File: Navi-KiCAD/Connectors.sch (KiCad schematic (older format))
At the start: 4 parts, among them J1 AXK5S80047YG, J2 AXK5S80047YG, J3 473460001, U13 NUF2042XV6T1G

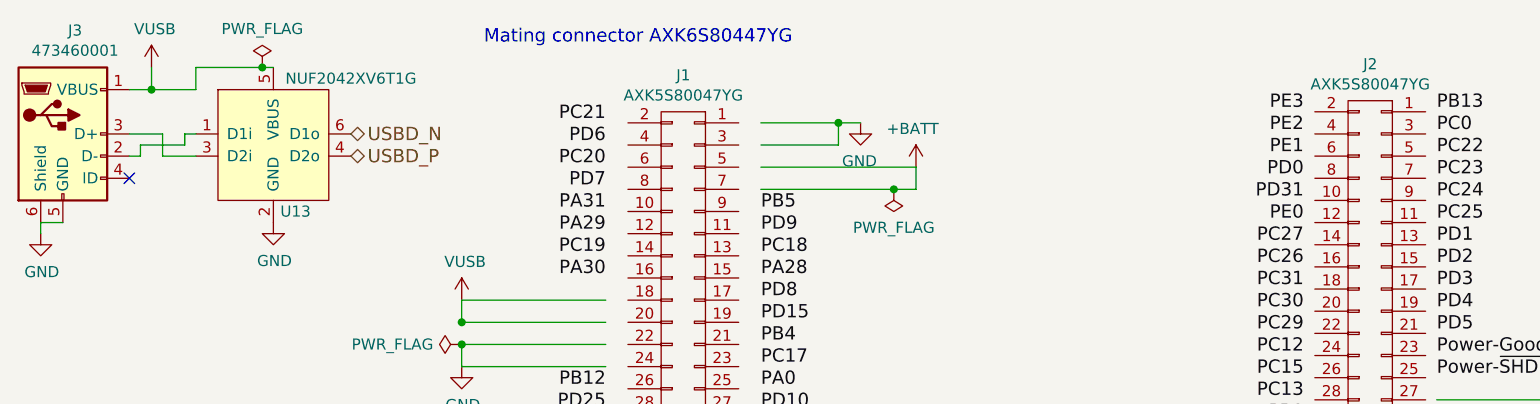
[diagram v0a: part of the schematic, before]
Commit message: Completed key routing.
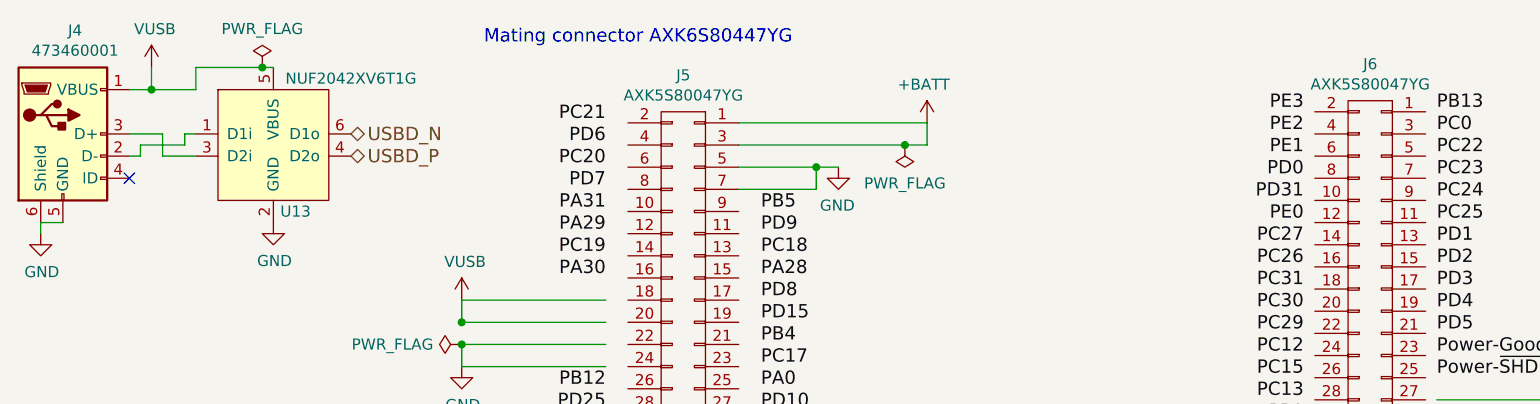
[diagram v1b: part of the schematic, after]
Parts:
- renumbered J3 to J4, J1 to J5, J2 to J6
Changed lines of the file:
@@
 $EndDescr
 $Comp
-L USB_OTG J3
+L USB_OTG J4
 U 1 1 58B53909
 P 1200 1450
-F 0 "J3" H 1255 1917 50  0000 C CNN
+F 0 "J4" H 1255 1917 50  0000 C CNN
 F 1 "473460001" H 1255 1826 50  0000 C CNN
 F 2 "Connectors:USB_Micro-B_0473460001" H -3450 -1350 50  0001 C CNN
@@
 $EndComp
 $Comp
-L CONN_02X40 J1
+L CONN_02X40 J5
 U 1 1 58B54687
 P 4000 3350
-F 0 "J1" H 4000 5515 50  0000 C CNN
+F 0 "J5" H 4000 5515 50  0000 C CNN
 F 1 "AXK5S80047YG" H 4000 5424 50  0000 C CNN
 F 2 "Connectors:AXK5S80047YG" H -550 200 50  0001 C CNN
@@
 Mating connector AXK6S80447YG
 $Comp
-L CONN_02X40 J2
+L CONN_02X40 J6
 U 1 1 58B24420
 P 7100 3300
-F 0 "J2" H 7100 5465 50  0000 C CNN
+F 0 "J6" H 7100 5465 50  0000 C CNN
 F 1 "AXK5S80047YG" H 7100 5374 50  0000 C CNN
 F 2 "Connectors:AXK5S80047YG" H 2550 150 50  0001 C CNN
@@
 L +BATT #PWR0154
 U 1 1 58DB91A4
-P 5050 1600
-F 0 "#PWR0154" H 4000 -1300 50  0001 C CNN
-F 1 "+BATT" H 5065 1773 50  0000 C CNN
-F 2 "" H 4000 -1150 50  0001 C CNN
-F 3 "" H 4000 -1150 50  0001 C CNN
-	1    5050 1600
+P 5100 1400
+F 0 "#PWR0154" H 4050 -1500 50  0001 C CNN
+F 1 "+BATT" H 5115 1573 50  0000 C CNN
+F 2 "" H 4050 -1350 50  0001 C CNN
+F 3 "" H 4050 -1350 50  0001 C CNN
+	1    5100 1400
 	-1   0    0    -1
 $EndComp
@@
 L GND #PWR0155
 U 1 1 58DD26EA
-P 4800 1400
-F 0 "#PWR0155" H 850 -2300 50  0001 C CNN
-F 1 "GND" H 4805 1227 50  0000 C CNN
-F 2 "" H 850 -2050 50  0001 C CNN
-F 3 "" H 850 -2050 50  0001 C CNN
-	1    4800 1400
+P 4700 1600
+F 0 "#PWR0155" H 750 -2100 50  0001 C CNN
+F 1 "GND" H 4705 1427 50  0000 C CNN
+F 2 "" H 750 -1850 50  0001 C CNN
+F 3 "" H 750 -1850 50  0001 C CNN
+	1    4700 1600
 	-1   0    0    -1
 $EndComp
@@
 PC7
 Wire Wire Line
-	4700 1500 4350 1500
-Wire Wire Line
-	4350 1400 4800 1400
-Wire Wire Line
-	4700 1400 4700 1500
-Wire Wire Line
-	4350 1700 5050 1700
-Wire Wire Line
-	5050 1700 5050 1600
-Connection ~ 4700 1400
+	4600 1700 4250 1700
+Wire Wire Line
+	4250 1600 4700 1600
+Wire Wire Line
+	4600 1600 4600 1700
+Wire Wire Line
+	4250 1500 5100 1500
+Wire Wire Line
+	5100 1500 5100 1400
+Connection ~ 4600 1600
 Text Label 7400 3450 0    60   ~ 0
 900-DIO-10
@@
 L PWR_FLAG #FLG0158
 U 1 1 58BE5320
-P 4950 1700
-F 0 "#FLG0158" H -700 275 50  0001 C CNN
-F 1 "PWR_FLAG" H 4950 1873 50  0000 C CNN
-F 2 "" H -700 200 50  0001 C CNN
-F 3 "" H -700 200 50  0001 C CNN
-	1    4950 1700
+P 5000 1500
+F 0 "#FLG0158" H -650 75  50  0001 C CNN
+F 1 "PWR_FLAG" H 5000 1673 50  0000 C CNN
+F 2 "" H -650 0   50  0001 C CNN
+F 3 "" H -650 0   50  0001 C CNN
+	1    5000 1500
 	-1   0    0    1
 $EndComp
-Connection ~ 4950 1700
+Connection ~ 5000 1500
 $Comp
 L PWR_FLAG #FLG0159
@@
 	1750 1450 1800 1450
 Wire Wire Line
-	5050 1600 4350 1600
+	5100 1400 4250 1400
 $EndSCHEMATC

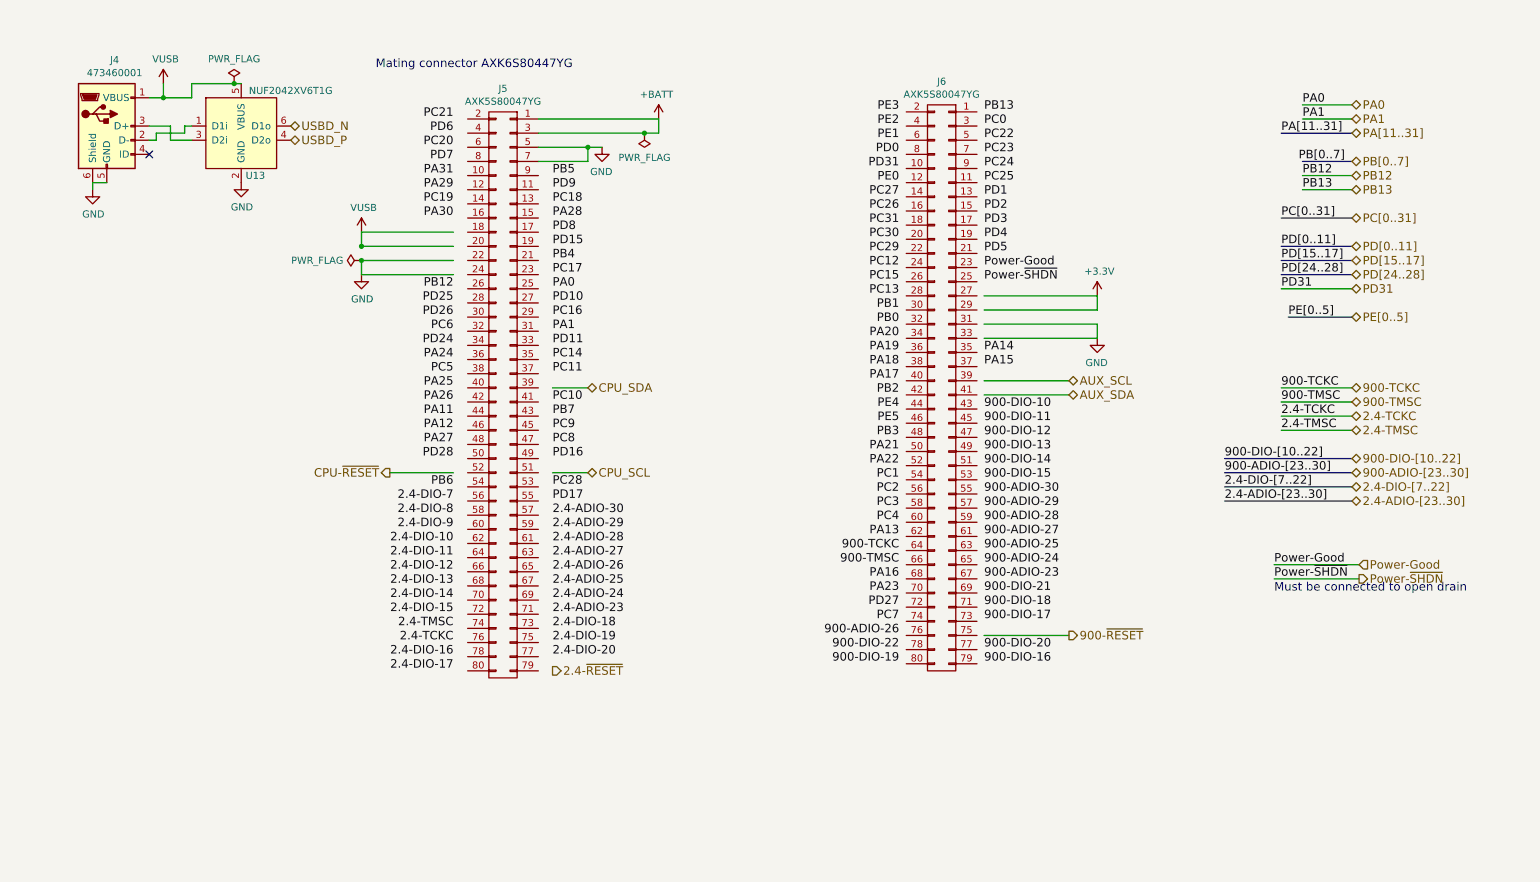
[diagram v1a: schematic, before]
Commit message: Some more GNC processor routing
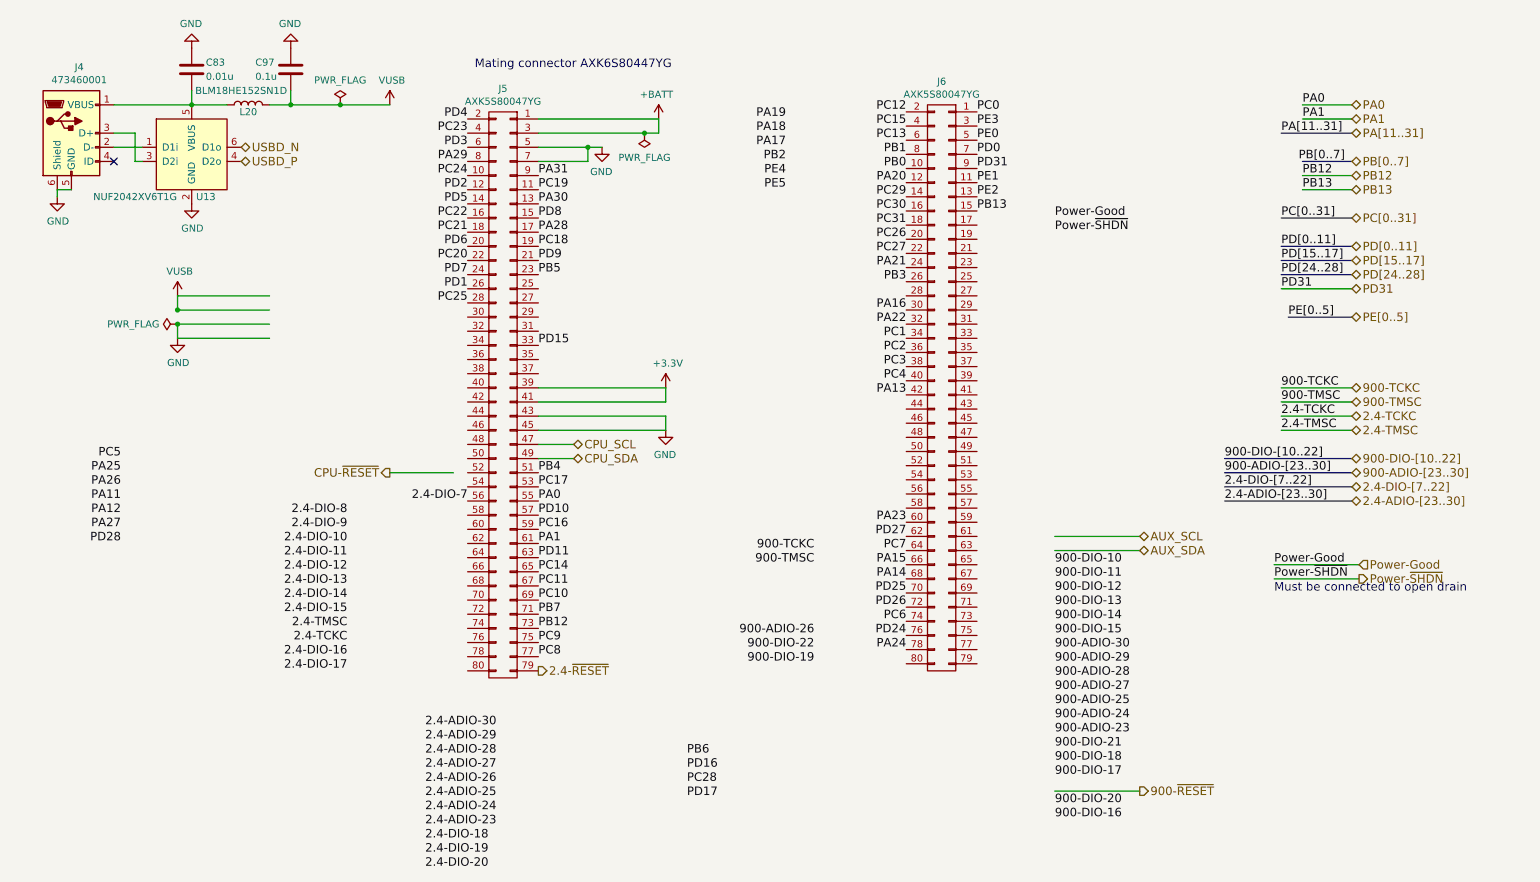
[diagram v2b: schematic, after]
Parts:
- added C83: 0.01u, Capacitors_SMD:C_0402, symbol C
- added C97: 0.1u, Capacitors_SMD:C_0402, symbol C
- added L20: BLM18HE152SN1D, Inductors_SMD:L_0603, symbol L
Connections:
- wire segments 49 -> 46
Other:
- moved on the sheet: J4, U13

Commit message: Additional routing
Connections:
- net labels removed: Power-Good
- wire segments 46 -> 42
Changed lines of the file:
@@
 Text HLabel 2150 1600 2    60   BiDi ~ 0
 USBD_N
-Text HLabel 3200 3900 0    60   Output ~ 0
+Text HLabel 2450 4050 0    60   Output ~ 0
 CPU-~RESET
-Text HLabel 8500 6150 2    60   Output ~ 0
+Text HLabel 8950 6100 2    60   Output ~ 0
 900-~RESET
 Text HLabel 4250 5300 2    60   Output ~ 0
@@
 Text HLabel 10000 2600 2    60   BiDi ~ 0
 PD31
-Text HLabel 8500 4450 2    60   BiDi ~ 0
+Text HLabel 5650 2250 2    60   BiDi ~ 0
 AUX_SDA
-Text HLabel 8500 4350 2    60   BiDi ~ 0
+Text HLabel 5650 2150 2    60   BiDi ~ 0
 AUX_SCL
 Text HLabel 4500 3800 2    60   BiDi ~ 0
@@
 Text HLabel 10000 4100 2    60   BiDi ~ 0
 2.4-ADIO-[23..30]
-Wire Wire Line
-	9450 4550 10050 4550
-Text Label 9450 4550 0    60   ~ 0
-Power-Good
-Text HLabel 10050 4550 2    60   Input ~ 0
-Power-Good
 Text Label 9450 4650 0    60   ~ 0
 Power-~SHDN
@@
 	-1   0    0    -1
 $EndComp
-Text Label 7900 5250 0    60   ~ 0
+Text Label 7350 5150 0    60   ~ 0
 900-ADIO-29
-Text Label 7900 5150 0    60   ~ 0
+Text Label 7350 5050 0    60   ~ 0
 900-ADIO-30
-Text Label 7900 5350 0    60   ~ 0
+Text Label 7350 5250 0    60   ~ 0
 900-ADIO-28
-Text Label 6200 5050 2    60   ~ 0
+Text Label 7350 4550 0    60   ~ 0
 900-ADIO-26
-Text Label 7900 5650 0    60   ~ 0
+Text Label 7350 4350 0    60   ~ 0
 900-ADIO-24
-Text Label 7900 5750 0    60   ~ 0
+Text Label 7350 4250 0    60   ~ 0
 900-ADIO-23
-Text Label 7900 5450 0    60   ~ 0
+Text Label 7350 4150 0    60   ~ 0
 900-ADIO-27
-Text Label 7900 5550 0    60   ~ 0
+Text Label 7350 4650 0    60   ~ 0
 900-ADIO-25
-Text Label 2900 4200 2    60   ~ 0
+Text Label 3750 4000 2    60   ~ 0
 2.4-DIO-8
-Text Label 2900 4300 2    60   ~ 0
+Text Label 3750 3900 2    60   ~ 0
 2.4-DIO-9
-Text Label 2900 4400 2    60   ~ 0
+Text Label 3750 3800 2    60   ~ 0
 2.4-DIO-10
-Text Label 2900 4500 2    60   ~ 0
+Text Label 3750 4300 2    60   ~ 0
 2.4-DIO-11
-Text Label 2900 4600 2    60   ~ 0
+Text Label 3750 4500 2    60   ~ 0
 2.4-DIO-12
-Text Label 2900 4700 2    60   ~ 0
+Text Label 3750 4700 2    60   ~ 0
 2.4-DIO-13
-Text Label 2900 4800 2    60   ~ 0
+Text Label 3750 4900 2    60   ~ 0
 2.4-DIO-14
-Text Label 2900 4900 2    60   ~ 0
+Text Label 3750 5300 2    60   ~ 0
 2.4-DIO-15
-Text Label 2900 5100 2    60   ~ 0
+Text Label 3750 5100 2    60   ~ 0
 2.4-TCKC
-Text Label 2900 5000 2    60   ~ 0
+Text Label 3750 5200 2    60   ~ 0
 2.4-TMSC
-Text Label 2900 5200 2    60   ~ 0
+Text Label 3750 5000 2    60   ~ 0
 2.4-DIO-16
-Text Label 2900 5300 2    60   ~ 0
+Text Label 3750 4800 2    60   ~ 0
 2.4-DIO-17
-Text Label 3450 6500 0    60   ~ 0
+Text Label 3750 4600 2    60   ~ 0
 2.4-DIO-18
-Text Label 3450 6600 0    60   ~ 0
+Text Label 3750 4400 2    60   ~ 0
 2.4-DIO-19
-Text Label 3450 6700 0    60   ~ 0
+Text Label 3750 4200 2    60   ~ 0
 2.4-DIO-20
-Text Label 3450 6400 0    60   ~ 0
+Text Label 1250 3750 2    60   ~ 0
 2.4-ADIO-23
-Text Label 3450 6300 0    60   ~ 0
+Text Label 1250 3850 2    60   ~ 0
 2.4-ADIO-24
-Text Label 3450 6200 0    60   ~ 0
+Text Label 1250 3950 2    60   ~ 0
 2.4-ADIO-25
-Text Label 3450 6100 0    60   ~ 0
+Text Label 1250 4050 2    60   ~ 0
 2.4-ADIO-26
-Text Label 3450 6000 0    60   ~ 0
+Text Label 1250 4150 2    60   ~ 0
 2.4-ADIO-27
-Text Label 3450 5900 0    60   ~ 0
+Text Label 1250 4250 2    60   ~ 0
 2.4-ADIO-28
-Text Label 3450 5800 0    60   ~ 0
+Text Label 1250 4350 2    60   ~ 0
 2.4-ADIO-29
-Text Label 3450 5700 0    60   ~ 0
+Text Label 1250 4450 2    60   ~ 0
 2.4-ADIO-30
 Text Label 5300 6200 0    60   ~ 0
@@
 Text Label 6850 1850 2    60   ~ 0
 PA20
-Text Label 6000 1400 2    60   ~ 0
+Text Label 5650 1450 2    60   ~ 0
 PA19
-Text Label 6000 1500 2    60   ~ 0
+Text Label 5650 1550 2    60   ~ 0
 PA18
-Text Label 6000 1600 2    60   ~ 0
+Text Label 5650 1650 2    60   ~ 0
 PA17
-Text Label 6000 1700 2    60   ~ 0
+Text Label 5650 1750 2    60   ~ 0
 PB2
-Text Label 6000 1800 2    60   ~ 0
+Text Label 5650 1850 2    60   ~ 0
 PE4
-Text Label 6000 1900 2    60   ~ 0
+Text Label 6850 2650 2    60   ~ 0
 PE5
 Text Label 6850 2550 2    60   ~ 0
@@
 Text Label 6850 2450 2    60   ~ 0
 PA21
-Text Label 7900 6350 0    60   ~ 0
+Text Label 8350 6300 0    60   ~ 0
 900-DIO-16
-Text Label 7900 6250 0    60   ~ 0
+Text Label 8350 6200 0    60   ~ 0
 900-DIO-20
 Wire Wire Line
-	7900 6150 8500 6150
-Text Label 7900 5850 0    60   ~ 0
+	8350 6100 8950 6100
+Text Label 7350 3950 0    60   ~ 0
 900-DIO-21
-Text Label 7900 6050 0    60   ~ 0
+Text Label 8350 6000 0    60   ~ 0
 900-DIO-17
-Text Label 7900 5950 0    60   ~ 0
+Text Label 8350 5900 0    60   ~ 0
 900-DIO-18
-Text Label 6200 5150 2    60   ~ 0
+Text Label 7350 4050 0    60   ~ 0
 900-DIO-22
-Text Label 6200 5250 2    60   ~ 0
+Text Label 8150 6300 2    60   ~ 0
 900-DIO-19
 Text Label 3750 2700 2    60   ~ 0
@@
 Text Label 6850 2750 2    60   ~ 0
 PA16
-Text Label 6200 4450 2    60   ~ 0
+Text Label 8150 5900 2    60   ~ 0
 900-TCKC
-Text Label 6200 4550 2    60   ~ 0
+Text Label 8150 6000 2    60   ~ 0
 900-TMSC
 Text Label 6850 4250 2    60   ~ 0
@@
 	5100 1500 5100 1400
 Connection ~ 4600 1600
-Text Label 7900 4550 0    60   ~ 0
+Text Label 8350 5200 0    60   ~ 0
 900-DIO-10
-Text Label 7900 4650 0    60   ~ 0
+Text Label 8350 5300 0    60   ~ 0
 900-DIO-11
-Text Label 7900 4750 0    60   ~ 0
+Text Label 8350 5400 0    60   ~ 0
 900-DIO-12
-Text Label 7900 4850 0    60   ~ 0
+Text Label 8350 5500 0    60   ~ 0
 900-DIO-13
-Text Label 7900 4950 0    60   ~ 0
+Text Label 8350 5600 0    60   ~ 0
 900-DIO-14
-Text Label 7900 5050 0    60   ~ 0
+Text Label 8350 5700 0    60   ~ 0
 900-DIO-15
 Wire Wire Line
-	8500 4350 7900 4350
-Wire Wire Line
-	8500 4450 7900 4450
-Wire Wire Line
-	3650 3900 3200 3900
-Text Label 1300 4400 2    60   ~ 0
+	5650 2150 5050 2150
+Wire Wire Line
+	5650 2250 5050 2250
+Wire Wire Line
+	2900 4050 2450 4050
+Text Label 2250 6200 2    60   ~ 0
 PD28
-Text Label 1300 4300 2    60   ~ 0
+Text Label 2250 6100 2    60   ~ 0
 PA27
-Text Label 1300 4200 2    60   ~ 0
+Text Label 2250 6000 2    60   ~ 0
 PA12
-Text Label 1300 4100 2    60   ~ 0
+Text Label 2250 5900 2    60   ~ 0
 PA11
-Text Label 1300 4000 2    60   ~ 0
+Text Label 2250 5800 2    60   ~ 0
 PA26
-Text Label 1300 3900 2    60   ~ 0
+Text Label 2250 5700 2    60   ~ 0
 PA25
-Text Label 1300 3800 2    60   ~ 0
+Text Label 2250 5600 2    60   ~ 0
 PC5
 Text Label 6850 5150 2    60   ~ 0
@@
 Text Label 4250 5000 0    60   ~ 0
 PB12
-Text Label 7900 2100 0    60   ~ 0
-Power-Good
-Text Label 7900 2200 0    60   ~ 0
+Text Label 5050 2050 0    60   ~ 0
 Power-~SHDN
 Wire Wire Line
@@
 $EndComp
 Wire Wire Line
-	2350 2650 1700 2650
-Wire Wire Line
-	1700 2950 2350 2950
-Wire Wire Line
-	1700 2850 2350 2850
-Connection ~ 1700 2850
-Wire Wire Line
-	2350 2750 1700 2750
-Connection ~ 1700 2750
-$Comp
-L GND #PWR0159
-U 1 1 58BDD20C
-P 1700 2950
-F 0 "#PWR0159" H -2250 -750 50  0001 C CNN
-F 1 "GND" H 1705 2777 50  0000 C CNN
-F 2 "" H -2250 -500 50  0001 C CNN
-F 3 "" H -2250 -500 50  0001 C CNN
-	1    1700 2950
-	1    0    0    -1
-$EndComp
-$Comp
-L PWR_FLAG #FLG0160
+	4250 3100 4900 3100
+Wire Wire Line
+	4250 3200 4900 3200
+$Comp
+L PWR_FLAG #FLG0159
 U 1 1 58BE5320
 P 5000 1500
-F 0 "#FLG0160" H -650 75  50  0001 C CNN
+F 0 "#FLG0159" H -650 75  50  0001 C CNN
 F 1 "PWR_FLAG" H 5000 1673 50  0000 C CNN
 F 2 "" H -650 0   50  0001 C CNN
@@
 Connection ~ 5000 1500
 $Comp
-L PWR_FLAG #FLG0161
+L PWR_FLAG #FLG0160
 U 1 1 58BE5430
 P 2850 1300
-F 0 "#FLG0161" H -2800 -125 50  0001 C CNN
+F 0 "#FLG0160" H -2800 -125 50  0001 C CNN
 F 1 "PWR_FLAG" H 2850 1474 50  0000 C CNN
 F 2 "" H -2800 -200 50  0001 C CNN
@@
 $EndComp
 $Comp
-L PWR_FLAG #FLG0162
+L PWR_FLAG #FLG0161
 U 1 1 58BEF4A7
-P 1700 2850
-F 0 "#FLG0162" H -3950 1425 50  0001 C CNN
-F 1 "PWR_FLAG" V 1700 2978 50  0000 L CNN
-F 2 "" H -3950 1350 50  0001 C CNN
-F 3 "" H -3950 1350 50  0001 C CNN
-	1    1700 2850
-	0    -1   -1   0
-$EndComp
-Wire Wire Line
-	1700 2950 1700 2850
-Wire Wire Line
-	1700 2750 1700 2650
-$Comp
-L +3.3V #PWR0163
+P 5150 3500
+F 0 "#FLG0161" H -500 2075 50  0001 C CNN
+F 1 "PWR_FLAG" V 5150 3628 50  0000 L CNN
+F 2 "" H -500 2000 50  0001 C CNN
+F 3 "" H -500 2000 50  0001 C CNN
+	1    5150 3500
+	0    1    1    0
+$EndComp
+Wire Wire Line
+	4900 3200 4900 3100
+$Comp
+L +3.3V #PWR0162
 U 1 1 58BFD1FD
 P 5150 3300
-F 0 "#PWR0163" H 2150 1200 50  0001 C CNN
+F 0 "#PWR0162" H 2150 1200 50  0001 C CNN
 F 1 "+3.3V" H 5165 3473 50  0000 C CNN
 F 2 "" H 2150 1350 50  0001 C CNN
@@
 	5150 3400 5150 3300
 $Comp
-L VUSB #PWR0164
+L VUSB #PWR0163
 U 1 1 58E3762E
-P 1700 2650
-F 0 "#PWR0164" H -300 1250 50  0001 C CNN
-F 1 "VUSB" H 1715 2823 50  0000 C CNN
-F 2 "" H -300 1400 50  0001 C CNN
-F 3 "" H -300 1400 50  0001 C CNN
-	1    1700 2650
-	1    0    0    -1
+P 4900 3100
+F 0 "#PWR0163" H 2900 1700 50  0001 C CNN
+F 1 "VUSB" H 4915 3273 50  0000 C CNN
+F 2 "" H 2900 1850 50  0001 C CNN
+F 3 "" H 2900 1850 50  0001 C CNN
+	1    4900 3100
+	-1   0    0    -1
 $EndComp
 $Comp
@@
 $EndComp
 $Comp
-L GND #PWR0165
+L GND #PWR0164
 U 1 1 58E380BC
 P 1800 2000
-F 0 "#PWR0165" H -100 150 50  0001 C CNN
+F 0 "#PWR0164" H -100 150 50  0001 C CNN
 F 1 "GND" H 1805 1827 50  0000 C CNN
 F 2 "" H -100 400 50  0001 C CNN
@@
 Connection ~ 2850 1300
 $Comp
-L GND #PWR0166
+L GND #PWR0165
 U 1 1 58CFD68A
 P 1800 900
-F 0 "#PWR0166" H -100 -950 50  0001 C CNN
+F 0 "#PWR0165" H -100 -950 50  0001 C CNN
 F 1 "GND" H 1805 727 50  0000 C CNN
 F 2 "" H -100 -700 50  0001 C CNN
@@
 $EndComp
 $Comp
-L GND #PWR0167
+L GND #PWR0166
 U 1 1 58CFD6F1
 P 2500 900
-F 0 "#PWR0167" H 600 -950 50  0001 C CNN
+F 0 "#PWR0166" H 600 -950 50  0001 C CNN
 F 1 "GND" H 2505 727 50  0000 C CNN
 F 2 "" H 600 -700 50  0001 C CNN
